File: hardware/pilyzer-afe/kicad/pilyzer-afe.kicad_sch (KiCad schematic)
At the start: 32 parts, among them J5 Logic D0–D7 + GND, J6 Pico 2 socket, J7 Pico 2 socket, U1 TLV9064IDR, U2 TS5A23159DGSR

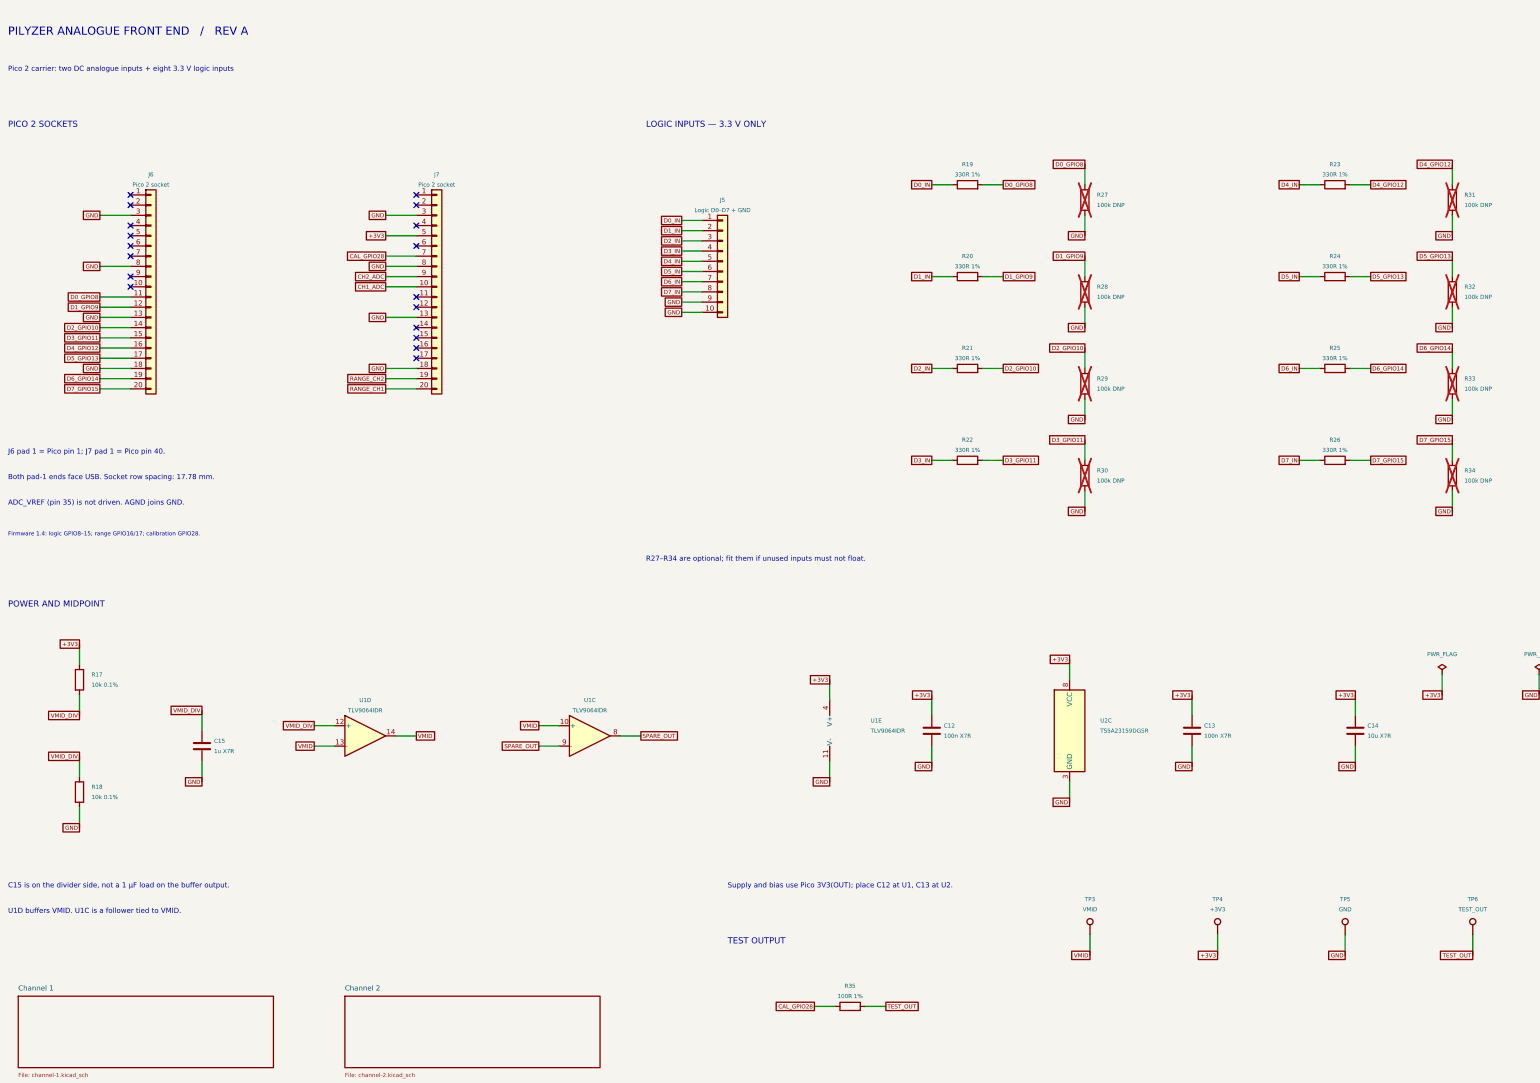
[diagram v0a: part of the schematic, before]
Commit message: Replace the passive RC pair with a Sallen-Key and drop the BNCs
A third channel divides the converter three ways instead of two, so
Nyquist fell from 124 to 82 kHz and the old passband reached past it:
between 82 kHz and roughly 250 kHz a signal was neither rejected by the
filter nor resolved by the converter, and folded back looking real.

Each channel now ends in a unity-gain Sallen-Key on U4 — R 2.67k, C1
2.2n, C2 1n to VMID — giving fc 40.2 kHz and Q 0.742, so 12.5 dB down at
three-channel Nyquist instead of nearly nothing. The shunt returns to
VMID rather than ground to keep the mid-rail bias ratiometric. R is a
value the board already used and the amplifier is a second TLV9064, so
the whole filter adds one part type to an order.

The BNC footprints are gone; inputs are the 2-pin headers. ERC is clean
and check_kicad.py covers the new topology.

Co-Authored-By: Claude Opus 5 <noreply@anthropic.com>
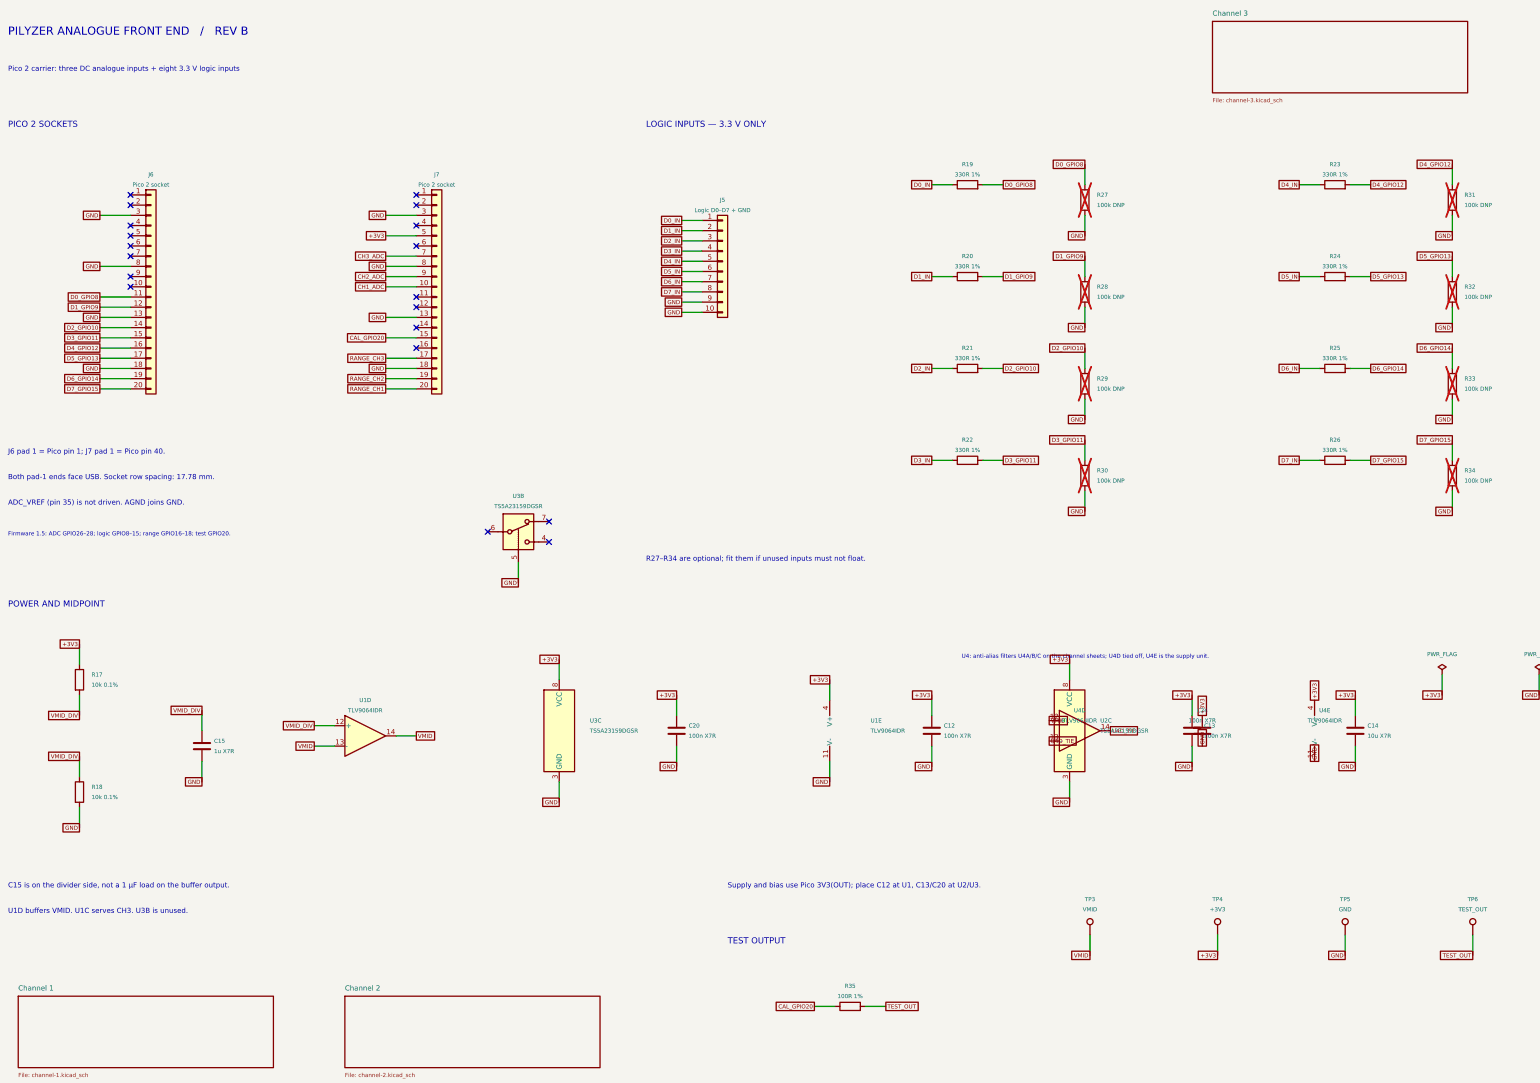
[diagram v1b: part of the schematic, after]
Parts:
- removed TP3: VMID, PiLyzer:TestPoint_Plated_Hole_D2.0mm, symbol PiLyzer:Connector_TestPoint
- removed TP4: +3V3, PiLyzer:TestPoint_Plated_Hole_D2.0mm, symbol PiLyzer:Connector_TestPoint
- removed unit 3 of U1
- added C20, C24: 100n X7R, PiLyzer:C_0603_1608Metric, symbol PiLyzer:Device_C
- added TP5: GND, PiLyzer:TestPoint_Plated_Hole_D2.0mm, symbol PiLyzer:Connector_TestPoint
- added TP6: TEST_OUT, PiLyzer:TestPoint_Plated_Hole_D2.0mm, symbol PiLyzer:Connector_TestPoint
- added U3: TS5A23159DGSR, PiLyzer:TSSOP-10_3x3mm_P0.5mm, symbol PiLyzer:Analog_Switch_TS5A23159DGS
- added U4: TLV9064IDR, PiLyzer:SOIC-14_3.9x8.7mm_P1.27mm, symbol PiLyzer:Amplifier_Operational_TLV9064
- TP3: renamed from TP5; value GND -> VMID
- TP4: renamed from TP6; value TEST_OUT -> +3V3
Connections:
- net +3V3: now also TP4.1, C20.1, C24.1, U3.8 (VCC), U4.4 (V+)
- net GND: now also C20.2, C24.2, TP5.1, U3.3 (GND), U3.5, U4.11 (V-); no longer TP3.1
- net TEST_OUT: now also TP6.1; no longer TP4.1
- net VMID: now also TP3.1, U4.12 (+)
- net CAL_GPIO20: now reaches J7.15 (Pin_15)
- net CAL_GPIO20: now also R35.1
- net RANGE_CH3: now reaches J7.17 (Pin_17)
- net CAL_GPIO28 renamed CH3_ADC
- net CH3_ADC: no longer R35.1
- new net U4D_TIE: U4.13 (-), U4.14
- no-connect marks 18 -> 19
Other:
- added sheet Channel 3 (channel-3.kicad_sch)
- note added: "Firmware 1.5: ADC GPIO26–28; logic GPIO8–15; range GPIO16–18; test GPIO20."
- note added: "PILYZER ANALOGUE FRONT END / REV B"
- note added: "Pico 2 carrier: three DC analogue inputs + eight 3.3 V logic inputs"
- note added: "Supply and bias use Pico 3V3(OUT); place C12 at U1, C13/C20 at U2/U3."
- note added: "U1D buffers VMID. U1C serves CH3. U3B is unused."
- note added: "U4: anti-alias filters U4A/B/C on the channel sheets; U4D tied off, U4E is the supply unit."
- note removed: "Firmware 1.4: logic GPIO8–15; range GPIO16/17; calibration GPIO28."
- note removed: "PILYZER ANALOGUE FRONT END / REV A"
- note removed: "Pico 2 carrier: two DC analogue inputs + eight 3.3 V logic inputs"
- note removed: "Supply and bias use Pico 3V3(OUT); place C12 at U1, C13 at U2."
- note removed: "U1D buffers VMID. U1C is a follower tied to VMID."
- moved on the sheet: TP3, TP4
